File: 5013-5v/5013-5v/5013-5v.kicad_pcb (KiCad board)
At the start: 2 copper layers, 33 parts, among them IC1 LM5013DDAR, J1 Conn_01x02_Pin, J2 Conn_01x02_Pin, J3 Conn_01x02_Pin, J4 Conn_01x02_Pin, U1 LT1084-5.0, U2 L7805

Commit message: 5013 rough layout complete
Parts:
- added C8: C_Polarized, Capacitor_THT:CP_Radial_D5.0mm_P2.00mm, F.Cu at (157.2, 102.4)
- added C9: C_Polarized, Capacitor_THT:CP_Radial_D5.0mm_P2.00mm, F.Cu at (163.3, 102.4)
- added R5: 2.2k, Resistor_SMD:R_0603_1608Metric_Pad0.98x0.95mm_HandSolder, F.Cu at (143.3, 118.5)
- added pgood1: LED, LED_SMD:LED_0603_1608Metric_Pad1.05x0.95mm_HandSolder, F.Cu at (141.5, 116.5)
- moved R3 51.4 mm to (270.1, 30.2)
- moved C1 51.4 mm to (245.5, 27.6)
- moved C6 47.5 mm to (270.4, 43.1)
- moved C4 45.8 mm to (247.7, 49.5)
- moved C2 45.4 mm to (250.6, 32.2)
- moved R2 41.6 mm to (252.1, 23.1)
- moved C7 40.9 mm to (269.4, 49.2)
- moved J3 38.5 mm to (277.8, 18.9), turned to 90 degrees
- moved C5 37.8 mm to (251.9, 55.3)
- moved R4 36.2 mm to (254.1, 49.2)
- moved J4 34.7 mm to (277.8, 23.5), turned to 90 degrees
- moved C3 34.6 mm to (269.4, 19.8)
- moved R1 34.1 mm to (252.3, 26.4)
- moved D3 34.0 mm to (280.8, 35.0), turned to 90 degrees
- moved U2 30.8 mm to (258.9, 60.7)
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- renumbered J4 to J2, J2 to J4
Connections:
- IC1 pad 6: unconnected-(IC1-PGOOD-Pad6) -> Net-(IC1-PGOOD)
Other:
- board text added: "2 side pcb consider 4 layer for extra heat sinking gnd planes"
- board text added: "consider vout on b.cu"

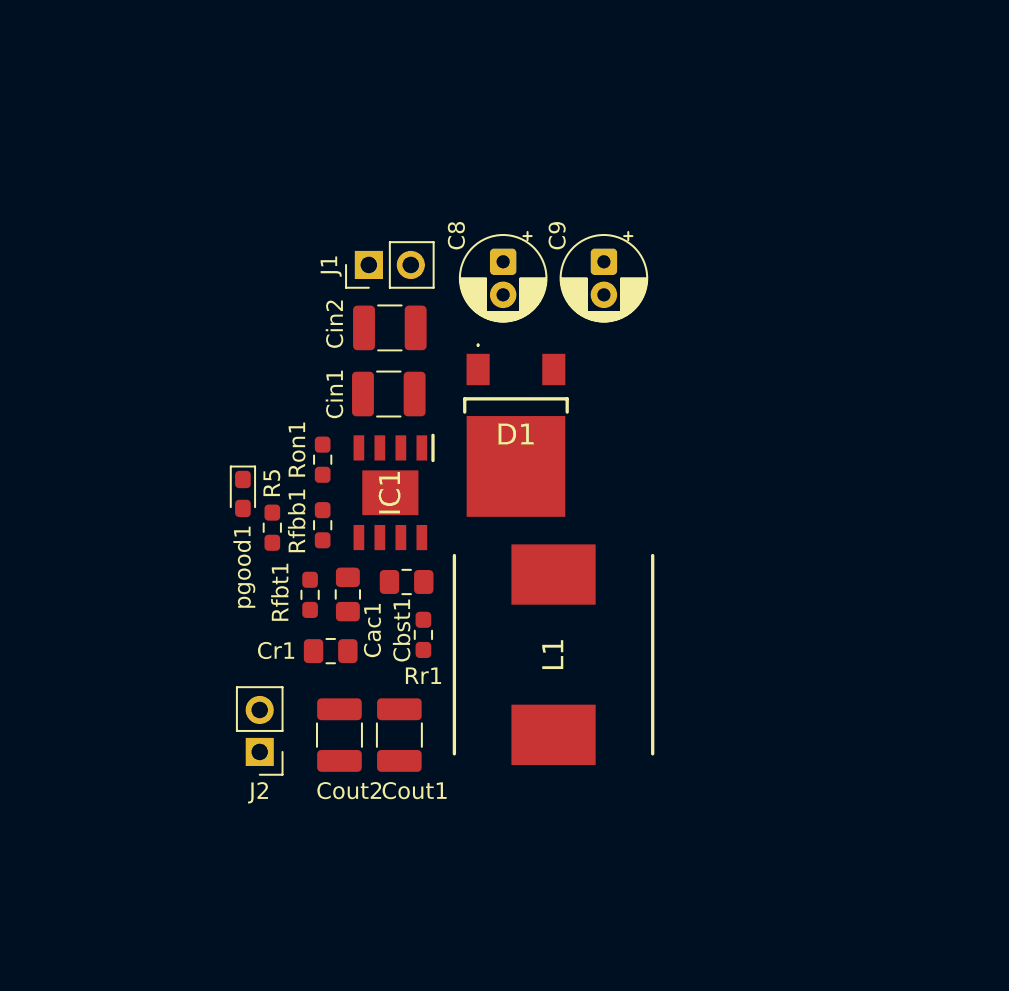
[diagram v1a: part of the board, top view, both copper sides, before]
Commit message: routed pcbnew, gathering bom
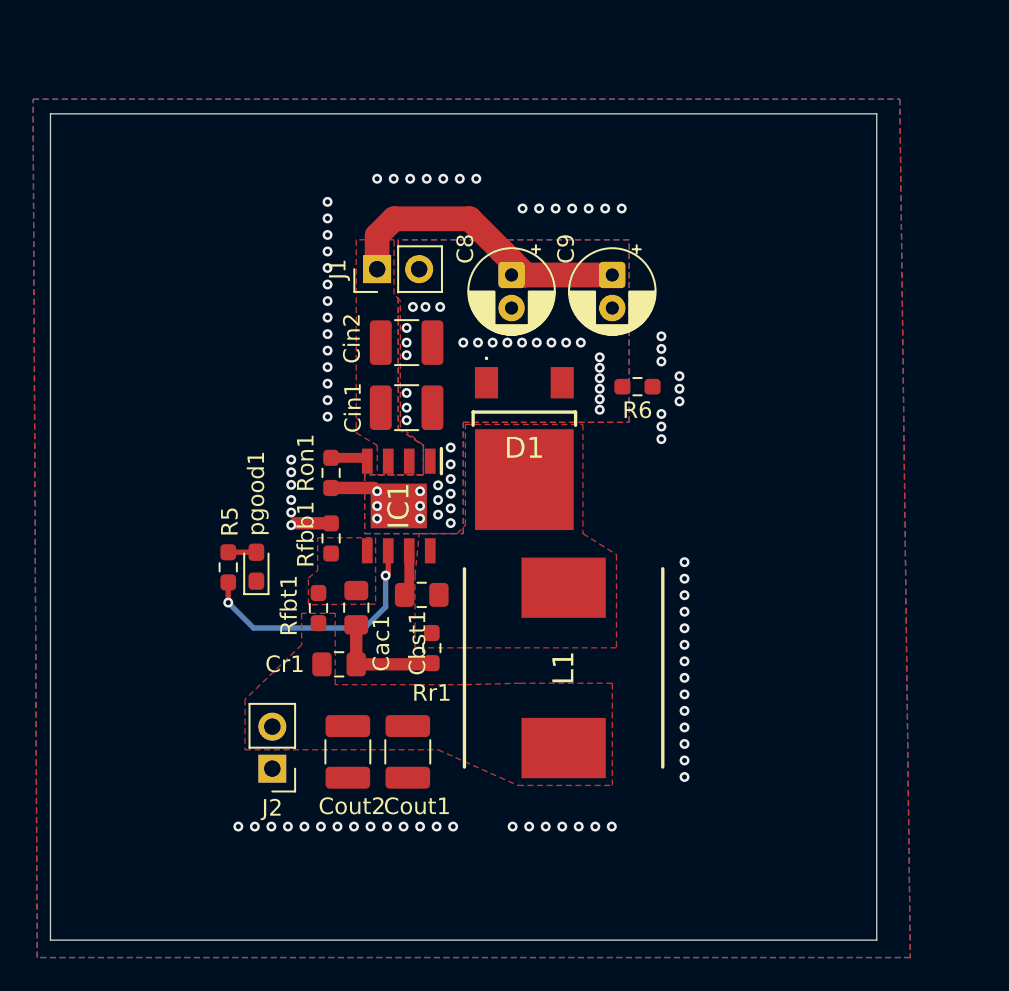
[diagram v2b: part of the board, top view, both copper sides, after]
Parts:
- added R6: 0, Resistor_SMD:R_0603_1608Metric_Pad0.98x0.95mm_HandSolder, F.Cu at (165.4, 110.0)
- moved pgood1 4.48 mm to (142.3, 120.9), turned to 90 degrees
- moved R5 3.59 mm to (140.6, 120.9)
- moved Cin1 1.36 mm to (151.4, 111.3)
- moved Cin2 1.35 mm to (151.4, 107.3)
- moved J2 1.27 mm to (143.3, 133.1)
- moved Cbst1 1.20 mm to (152.3, 122.6)
- moved Cout1 1.14 mm to (151.5, 132.1)
- moved Cout2 1.14 mm to (147.8, 132.1)
- moved L1 1.01 mm to (160.9, 127.0)
- moved D1 0.95 mm to (158.5, 113.9)
- moved C8 0.95 mm to (157.7, 103.2)
- moved C9 0.95 mm to (163.8, 103.2)
- moved Cac1 0.95 mm to (148.3, 123.4)
- moved Rfbb1 0.95 mm to (146.8, 119.2)
- moved Rfbt1 0.95 mm to (146.1, 123.4)
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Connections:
- net Net-(D1-K) renamed /sw
- net Net-(IC1-FB) renamed /fb
- C8 pad 2: GND -> GND1
- C9 pad 2: GND -> GND1
- Cin1 pad 2: GND -> GND1
- Cin2 pad 2: GND -> GND1
- D1 pad 2: GND -> GND1
- IC1 pad 1: GND -> GND1
- IC1 pad 9: GND -> GND1
- J1 pad 2: GND -> GND1
- Ron1 pad 2: GND -> GND1
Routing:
- net /Vin: track 0.00 -> 21.8 mm
- net Net-(IC1-PGOOD): track 0.00 -> 15.4 mm, vias 0 -> 2
- net Net-(Cac1-Pad1): track 0.00 -> 6.99 mm
- net GND1: track 0.00 -> 2.87 mm, vias 0 -> 39
- net Net-(IC1-BST): track 0.00 -> 2.79 mm
- net Net-(IC1-RON): track 0.00 -> 2.27 mm
- net GND: track 0.00 -> 2.16 mm, vias 0 -> 78
- net Net-(pgood1-A): track 0.00 -> 1.70 mm
- added copper zone on F.Cu, net /Vin
- added copper zone on F.Cu, net /Vout
- added copper zone on F.Cu, net /fb
- added copper zone on F.Cu, net /sw
- added copper zone on B.Cu, net GND
- added copper zone on F.Cu, net GND
- added copper zone on B.Cu, net GND1
- added copper zone on F.Cu, net GND1
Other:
- board outline added: 50 x 50 mm

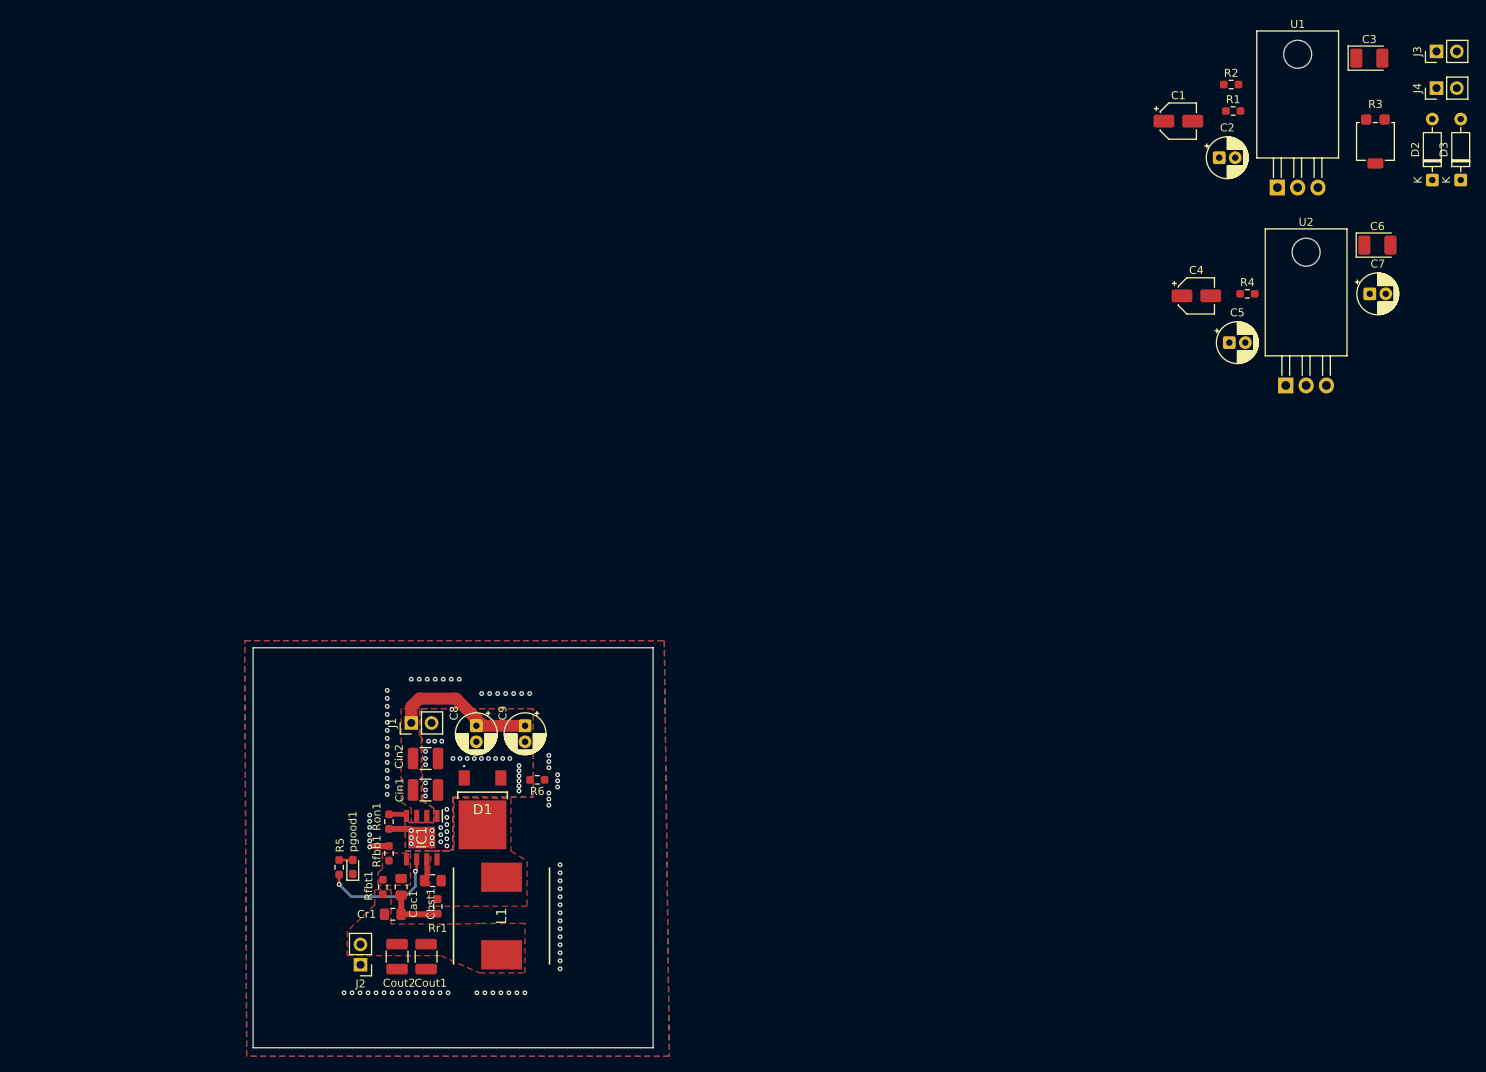
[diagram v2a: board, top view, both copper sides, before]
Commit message: added rev1BOM, fixed pours
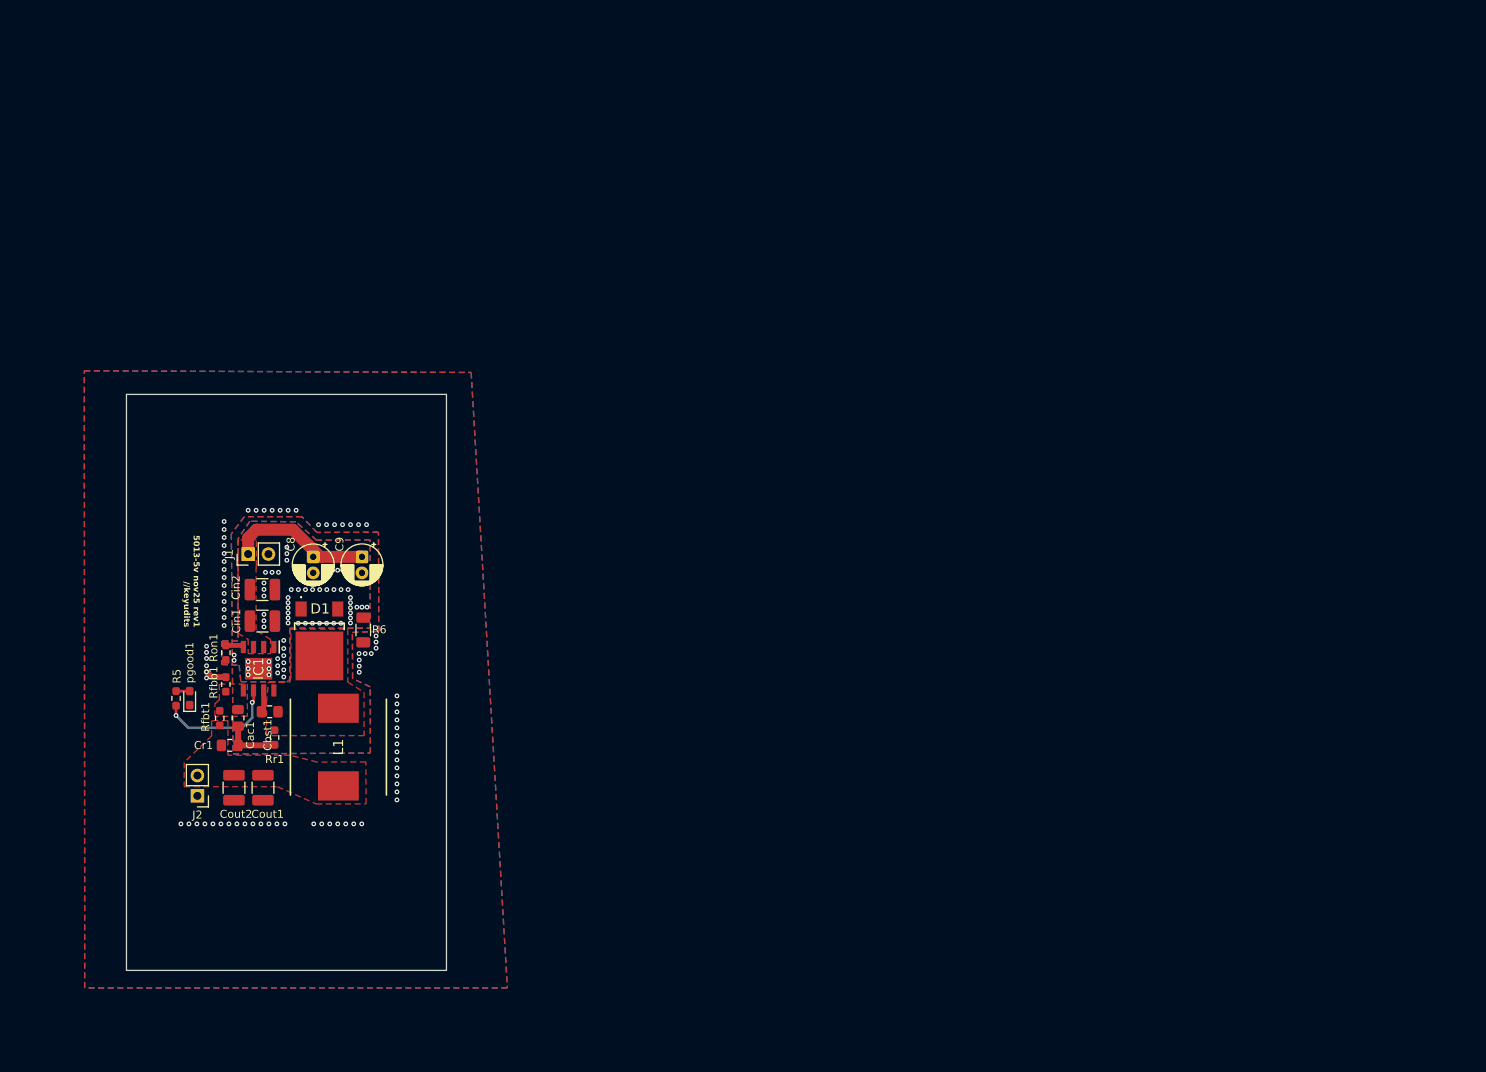
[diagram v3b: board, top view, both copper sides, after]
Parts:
- removed C1, C4: 10uF, Capacitor_SMD:CP_Elec_4x5.8
- removed C2, C5: 10uF, Capacitor_THT:CP_Radial_D5.0mm_P2.00mm
- removed C3, C6: 10uF_tantalum, Capacitor_Tantalum_SMD:CP_EIA-3528-12_Kemet-T_HandSolder
- removed C7: 0.1uF, Capacitor_THT:CP_Radial_D5.0mm_P2.00mm
- removed D2, D3: 1N4148, Diode_THT:D_DO-35_SOD27_P7.62mm_Horizontal
- removed J3, J4: Conn_01x02_Pin, Connector_PinHeader_2.54mm:PinHeader_1x02_P2.54mm_Vertical
- removed R1, R4: 0, Resistor_SMD:R_0603_1608Metric_Pad0.98x0.95mm_HandSolder
- removed R2: 121, Resistor_SMD:R_0603_1608Metric_Pad0.98x0.95mm_HandSolder
- removed R3: R_Variable, Potentiometer_SMD:Potentiometer_Bourns_3314G_Vertical
- removed U1: LT1084-5.0, Package_TO_SOT_THT:TO-220-3_Horizontal_TabDown
- removed U2: L7805, Package_TO_SOT_THT:TO-220-3_Horizontal_TabDown
- R6: footprint Resistor_SMD:R_0603_1608Metric_Pad0.98x0.95mm_HandSolder -> Resistor_SMD:R_1206_3216Metric_Pad1.30x1.75mm_HandSolder
- moved Cout1 29.4 mm to (131.1, 111.0)
- moved Cout2 29.4 mm to (127.4, 111.0)
- moved D1 29.4 mm to (138.1, 92.8)
- moved J1 29.4 mm to (129.2, 81.8)
- moved Cr1 29.4 mm to (126.9, 105.7)
- moved C8 29.4 mm to (137.3, 82.1)
- moved C9 29.4 mm to (143.4, 82.1)
- moved Cac1 29.4 mm to (127.9, 102.2)
- moved L1 29.4 mm to (140.5, 105.9)
- moved Rfbb1 29.4 mm to (126.4, 98.1)
- moved Rfbt1 29.4 mm to (125.7, 102.3)
- moved Ron1 29.4 mm to (126.4, 94.1)
- moved J2 29.4 mm to (122.9, 112.0)
- moved R5 29.4 mm to (120.2, 99.8)
- moved pgood1 29.4 mm to (121.9, 99.8)
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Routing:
- net GND1: track 2.87 -> 0.00 mm, vias 39 -> 63
- net GND: track 2.16 -> 2.68 mm
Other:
- board size 50 x 50 mm -> 40 x 72 mm
- board text added: "40x72mm 2mm safezone offset DIN rail carrier on-hand"
- board text added: "5013-5v nov25 rev1 //keyudits"
- board text added: "R6 location may be a problem"
- board text added: "vias to connect Fcu/Bcu gnd planes heat dissipation etc"

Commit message: plotted rev1 gerbers
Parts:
- added G***: LOGO, ear:nov25_4, F.Cu at (133.4, 128.0)
- added G***: LOGO, ear:nov25_4, F.Cu at (134.6, 67.0)
- renumbered Cin1 to Cin, Cin2 to Cin, Cout1 to Cout, Cout2 to Cout, Cr1 to Cr, Rfbb1 to Rfbb, Rfbt1 to Rfbt, Ron1 to Ron, Rr1 to Rr, J1 to Vin, J2 to Vout, Cac1 to cac, Cbst1 to cbst, pgood1 to pgood
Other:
- board text added: "+ -"
- board text added: "5vout"

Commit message: updated buildnote with testing results'
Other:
- board text added: "40x42mm 2mm safezone offset DIN rail carrier on-hand"
- board text added: "40x72mm 2mm safezone offset standard height DIN rail carrier"
- board text removed: "40x72mm 2mm safezone offset DIN rail carrier on-hand"
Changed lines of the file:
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@@
 		(fp_poly
 			(pts
-				(xy 0 -19) (xy 0 -19) (xy -0.022733 -19) (xy -0.069571 -19.060057) (xy -0.110344 -17.929676) (xy -0.141395 -16.543388)
+				(xy 0 -19) (xy -0.022733 -19) (xy -0.069571 -19.060057) (xy -0.110344 -17.929676) (xy -0.141395 -16.543388)
 				(xy -0.155522 -15.456695) (xy -0.163583 -13.74145) (xy -0.147228 -12.487077) (xy -0.100385 -11.614338)
 				(xy -0.016986 -11.04399) (xy 0.10904 -10.696794) (xy 0.220406 -10.549503) (xy 0.655097 -10.282329)
@@
 		(fp_poly
 			(pts
-				(xy 0 -19) (xy 0 -19) (xy -0.022733 -19) (xy -0.069571 -19.060057) (xy -0.110344 -17.929676) (xy -0.141395 -16.543388)
+				(xy 0 -19) (xy -0.022733 -19) (xy -0.069571 -19.060057) (xy -0.110344 -17.929676) (xy -0.141395 -16.543388)
 				(xy -0.155522 -15.456695) (xy -0.163583 -13.74145) (xy -0.147228 -12.487077) (xy -0.100385 -11.614338)
 				(xy -0.016986 -11.04399) (xy 0.10904 -10.696794) (xy 0.220406 -10.549503) (xy 0.655097 -10.282329)
@@
 	)
 	(gr_rect
+		(start 163.336 71.06)
+		(end 203.336 113.06)
+		(stroke
+			(width 0.1)
+			(type solid)
+		)
+		(fill no)
+		(layer "Dwgs.User")
+	)
+	(gr_rect
 		(start 114 61.8)
 		(end 154 133.8)
@@
 		)
 	)
+	(gr_text "40x42mm \n2mm safezone offset\nDIN rail carrier on-hand"
+		(at 179.46 68.774 0)
+		(layer "Cmts.User")
+		(effects
+			(font
+				(size 1 1)
+				(thickness 0.15)
+			)
+			(justify left bottom)
+		)
+	)
 	(gr_text "think about low side ground"
 		(at 77 148.06 0)
@@
 		)
 	)
-	(gr_text "40x72mm \n2mm safezone offset\nDIN rail carrier on-hand"
+	(gr_text "40x72mm \n2mm safezone offset\nstandard height DIN rail carrier "
 		(at 82.2 109.8 0)
 		(layer "Cmts.User")
